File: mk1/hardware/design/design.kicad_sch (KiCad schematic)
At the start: 28 parts, among them U1 Teensy4.1, U2 HM-TRP-868, U3 BMP390, U4 LSM6DSV80X, U5 LIS3MDL, U6 L80-R, U7 VN5E160STR, U8 VN5E160STR, U9 D36V6F3

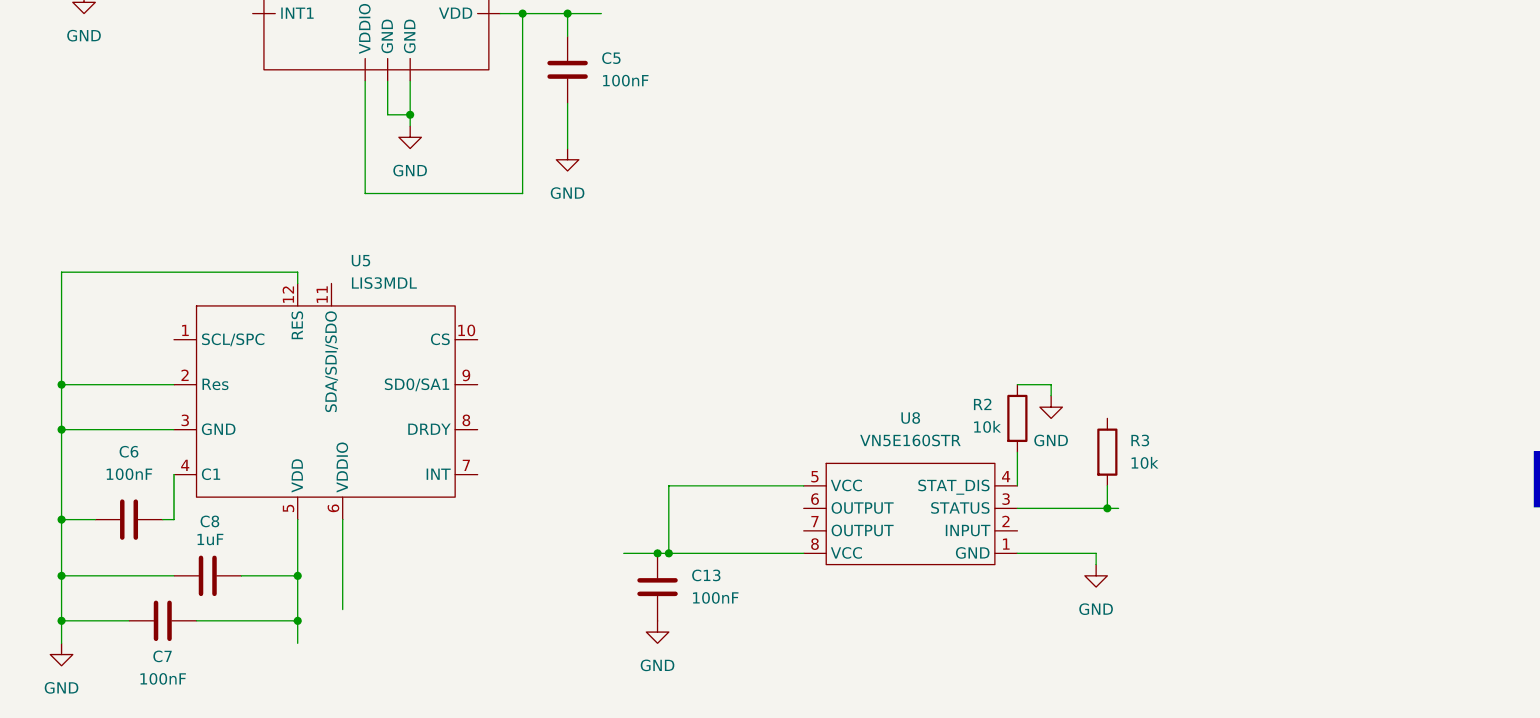
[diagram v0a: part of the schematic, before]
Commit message: Updated schematic to use different (available) magnetometer
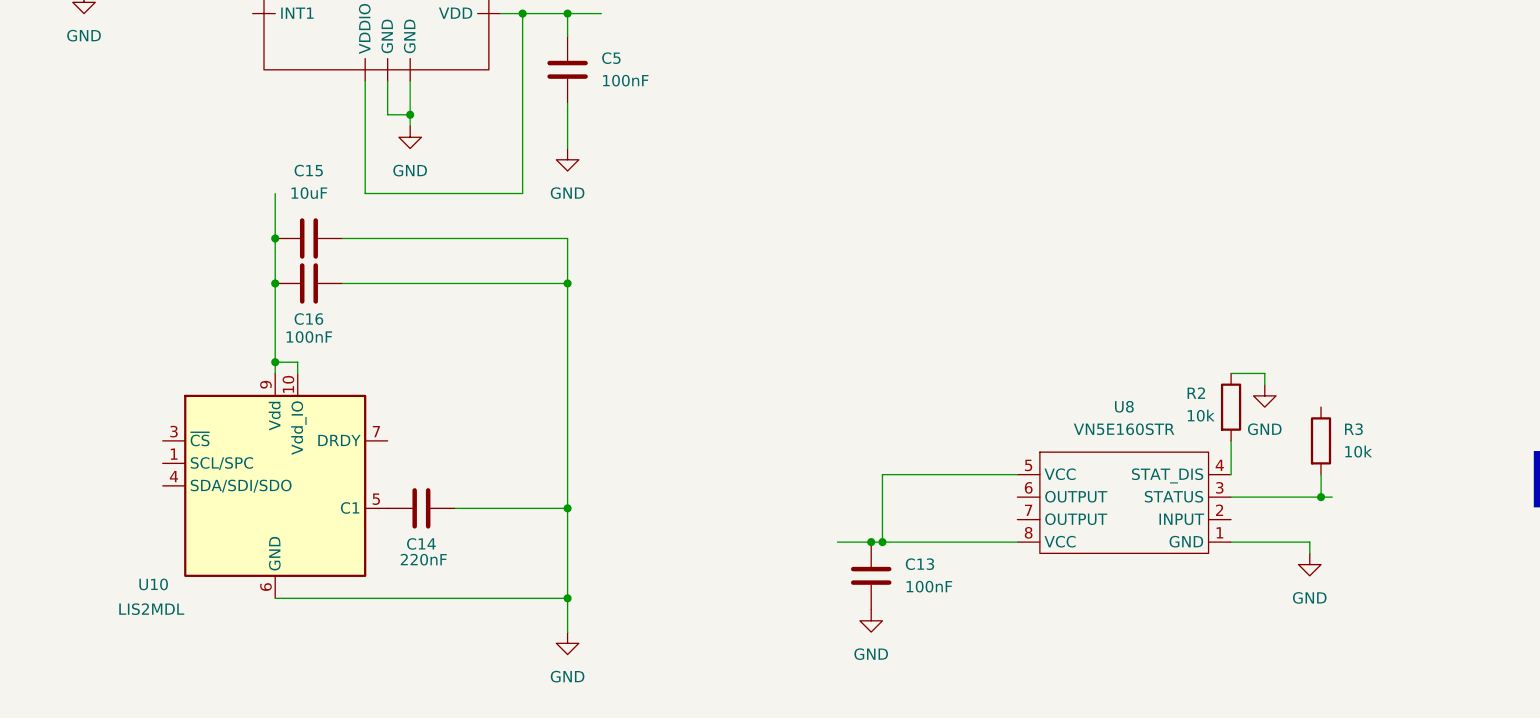
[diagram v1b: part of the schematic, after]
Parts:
- removed C6, C7: 100nF, symbol Device:C
- removed C8: 1uF, symbol Device:C
- removed U5: LIS3MDL, symbol rockety_extras:LIS3MDL
- added C14: 220nF, symbol Device:C
- added C15: 10uF, symbol Device:C
- added C16: 100nF, symbol Device:C
- added U10: LIS2MDL, Package_LGA:LGA-12_2x2mm_P0.5mm, symbol Sensor_Magnetic:LIS2MDL
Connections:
- net GND: now also C14.2, C15.2, C16.1, U10.6 (GND), U10.8 (GND)
- new net: C15.1, C16.2, U10.10 (Vdd_IO), U10.9 (Vdd)
- new net: C14.1, U10.5 (C1)
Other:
- moved on the sheet: C13, R2, R3, U8

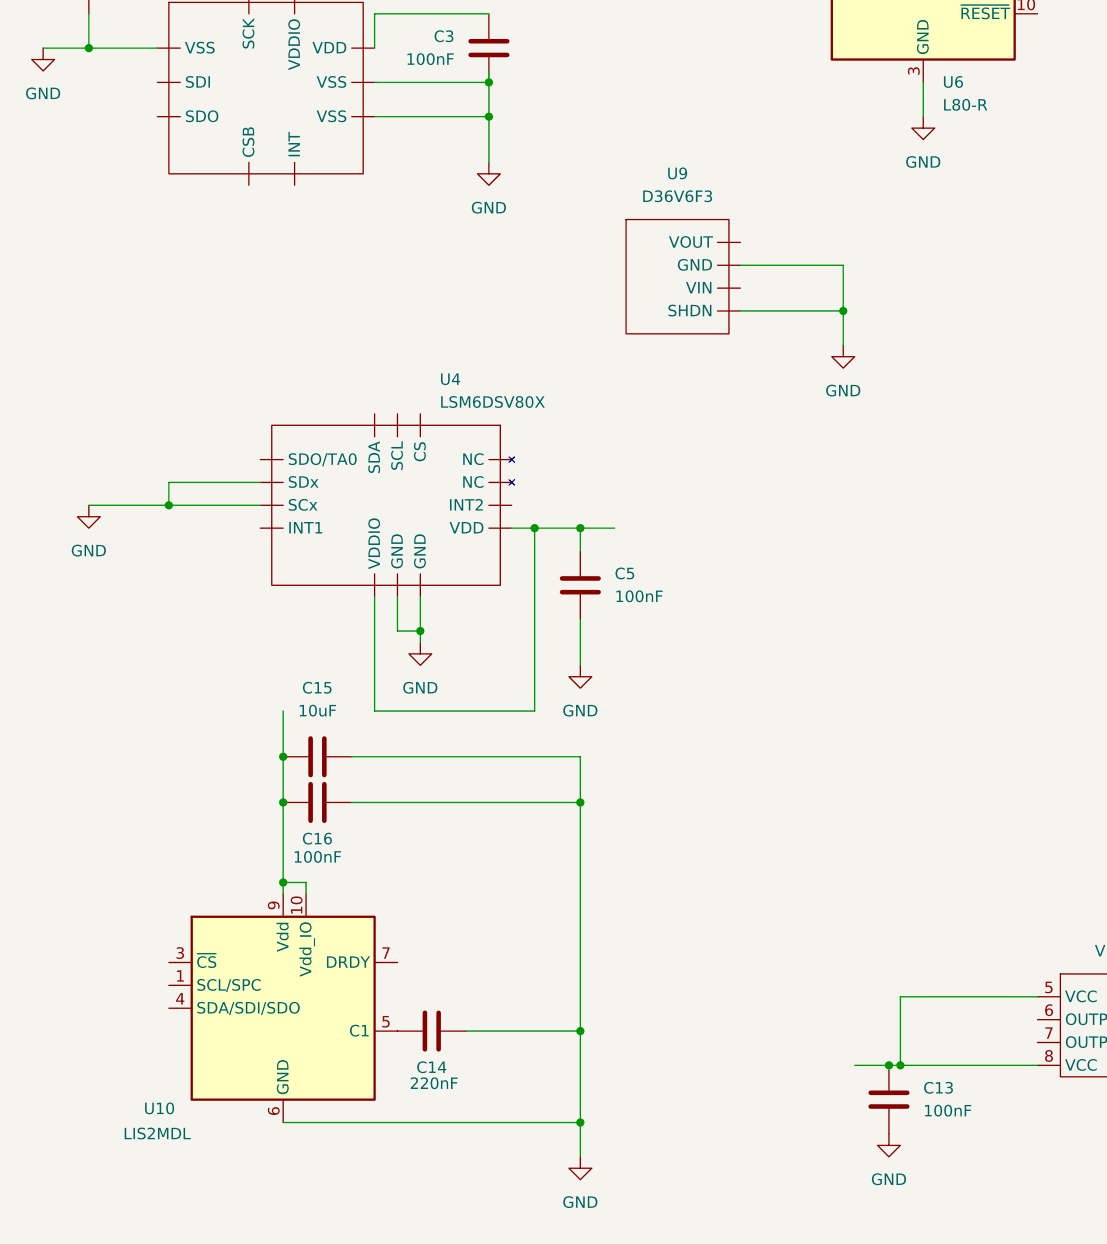
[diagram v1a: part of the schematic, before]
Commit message: Added symbol table, fixed magnetometer wiring
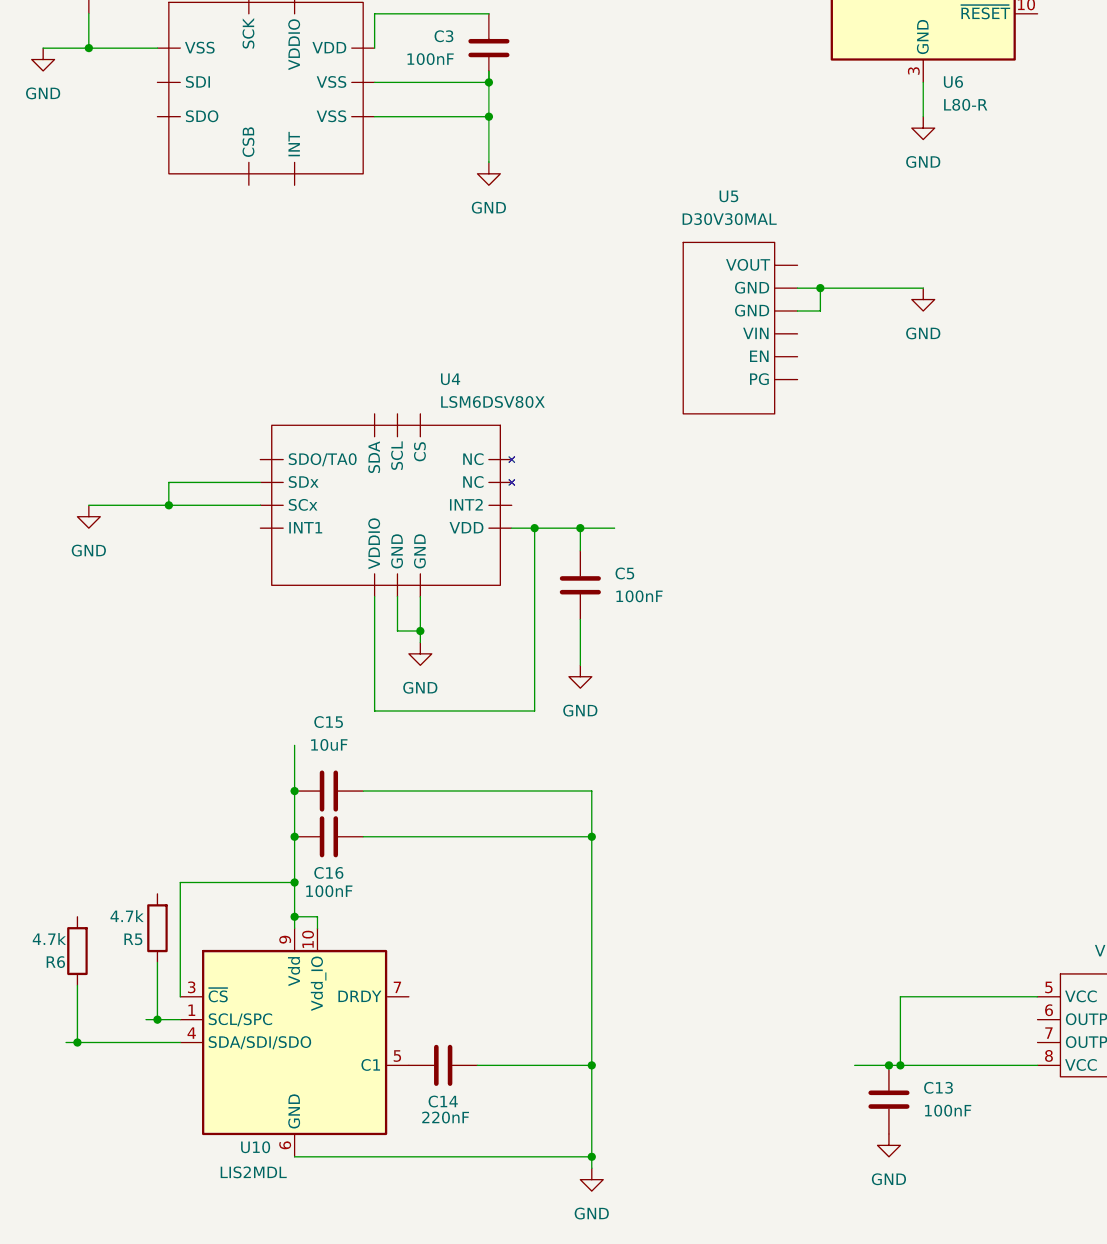
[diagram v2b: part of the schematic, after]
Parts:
- removed U9: D36V6F3, symbol rockety_extras:D36V6F3
- added R5, R6: 4.7k, symbol Device:R
- added U5: D30V30MAL, symbol rockety_extras:D30V30MAL
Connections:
- net GND: now also U5. (PG)
- net at C15.1, C16.2, U10.10 (Vdd_IO)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: now also U10.3 (~{CS})
- net at U10.1 (SCL/SPC): now also R5.1
- net at U10.4 (SDA/SDI/SDO): now also R6.1
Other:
- moved on the sheet: C14, C15, C16, U10
